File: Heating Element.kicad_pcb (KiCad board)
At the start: 2 copper layers, 56 x 37 mm, 20 parts, among them IC1 UCC23513QDWYRQ1, J1 Conn_01x04_Pin, U1 STP55NF06L, U2 MC7815CDTRKG

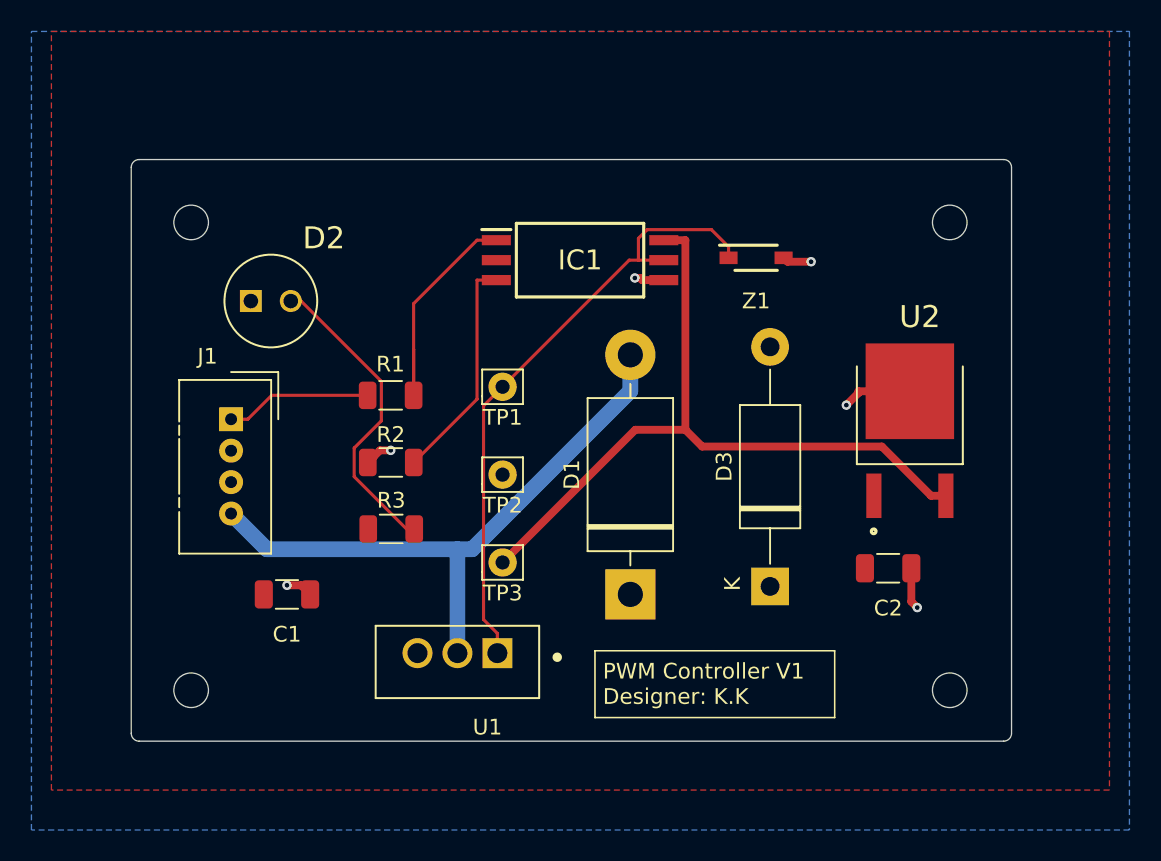
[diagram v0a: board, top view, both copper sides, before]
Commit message: Updated schematic and PCB
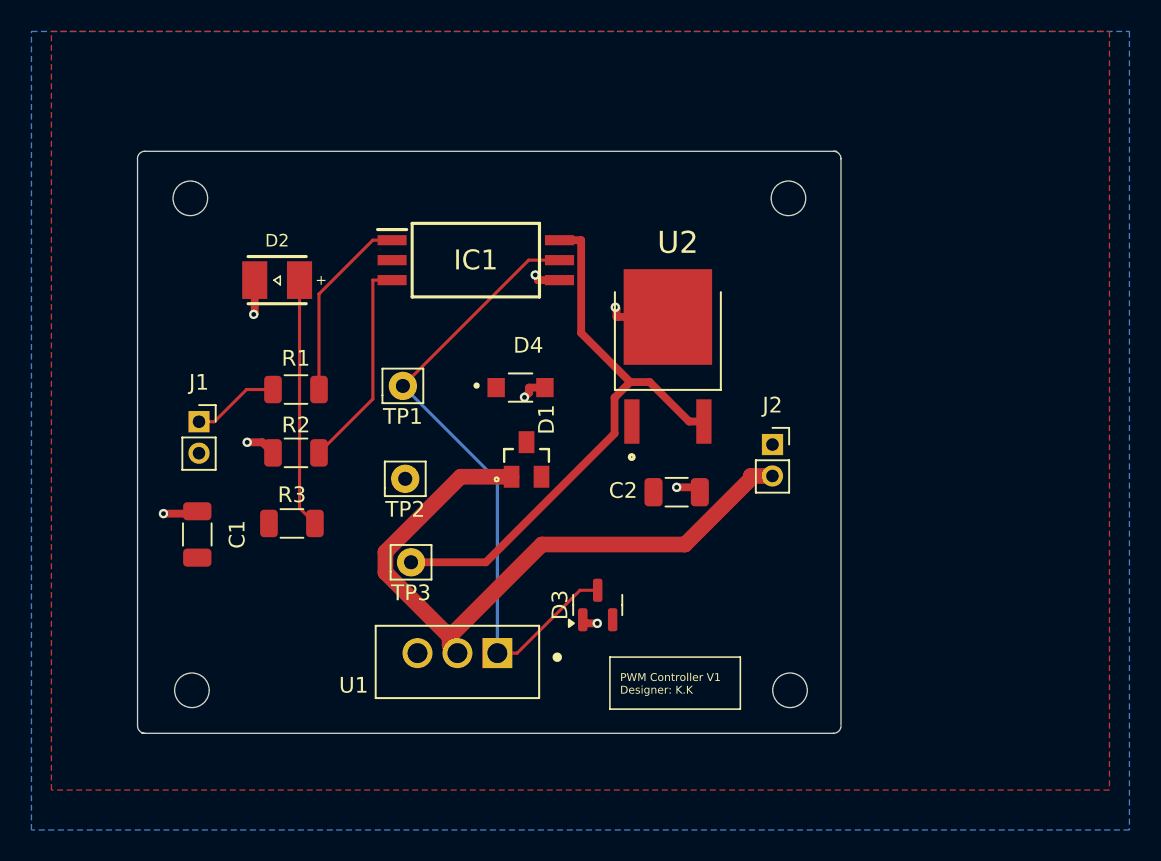
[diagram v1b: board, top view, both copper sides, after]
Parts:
- removed Z1: SZMMSZ5245BT1G, SZMMSZ5245BT1G_Kicad:SOD3716X135N
- added D4: BZD27C24P R3G, BZD27C10P:SODFL3618X143N, F.Cu at (120.0, 92.5)
- added J2: Conn_01x02_Pin, Connector_PinSocket_2.00mm:PinSocket_1x02_P2.00mm_Vertical, F.Cu at (136.0, 96.1)
- D1: value D -> PMEG3005ET-QR; footprint Diode_THT:D_DO-201AD_P15.24mm_Horizontal -> BAS70-7:SOT23
- D2: value L-53GD -> KA-3528SGT; footprint L-53GD:LEDRD254W50D500H1060 -> WL-SMTW_3528:WL-SMTW_3528
- D3: value D_Zener -> BZX84C15; footprint Diode_THT:D_DO-15_P15.24mm_Horizontal -> Package_TO_SOT_SMD:SOT-23
- J1: value Conn_01x04_Pin -> Conn_01x02_Pin; footprint Connector:NS-Tech_Grove_1x04_P2mm_Vertical -> Connector_PinSocket_2.00mm:PinSocket_1x02_P2.00mm_Vertical
- moved U2 16.1 mm to (129.4, 90.5)
- moved C2 14.3 mm to (129.9, 99.2)
- moved D3 11.0 mm to (124.9, 106.3)
- moved D1 10.8 mm to (120.4, 97.1)
- moved H2 10.4 mm to (137.1, 80.5)
- moved H4 10.2 mm to (137.2, 111.8)
- moved C1 6.86 mm to (99.5, 101.8), turned to 90 degrees
- moved IC1 6.63 mm to (117.2, 84.4)
- moved TP1 6.34 mm to (112.5, 92.4)
- moved R3 6.32 mm to (105.5, 101.2)
- moved TP2 6.20 mm to (112.7, 98.3)
- moved R2 6.06 mm to (105.7, 96.7)
- moved R1 6.03 mm to (105.7, 92.6)
- moved TP3 5.82 mm to (113.0, 103.6)
- moved J1 2.05 mm to (99.6, 94.7)
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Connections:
- D1 pad 1: +24V -> /Vdrain
- D1 pad 2: /Vdrain -> unconnected-(D1-Pad2)
- D3 pad 1: +24V -> GND
- D3 pad 2: GND -> unconnected-(D3-NC-Pad2)
- R3 pad 2: Net-(D2-PadA) -> Net-(D2-Pad2)
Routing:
- net Net-(D2-PadA): track 19.9 -> 0.00 mm
- net Net-(D2-Pad2): track 0.00 -> 15.9 mm
- net /+15V: track 46.9 -> 37.4 mm
- net /Vdrain: track 39.4 -> 43.2 mm
- net /PWM input: track 9.32 -> 5.56 mm
- net Net-(IC1-ANODE): track 15.7 -> 12.1 mm
- net GND: track 14.9 -> 16.5 mm, vias 6 -> 8
- net /VG: track 39.9 -> 40.8 mm
- net Net-(IC1-CATHODE): track 14.5 -> 13.6 mm
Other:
- board size 56 x 37 mm -> 44.8 x 37 mm

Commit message: Updated Schematic components (all smd) Updated PCB layout (includes schematic changes and routing) Updtaed Gerber files
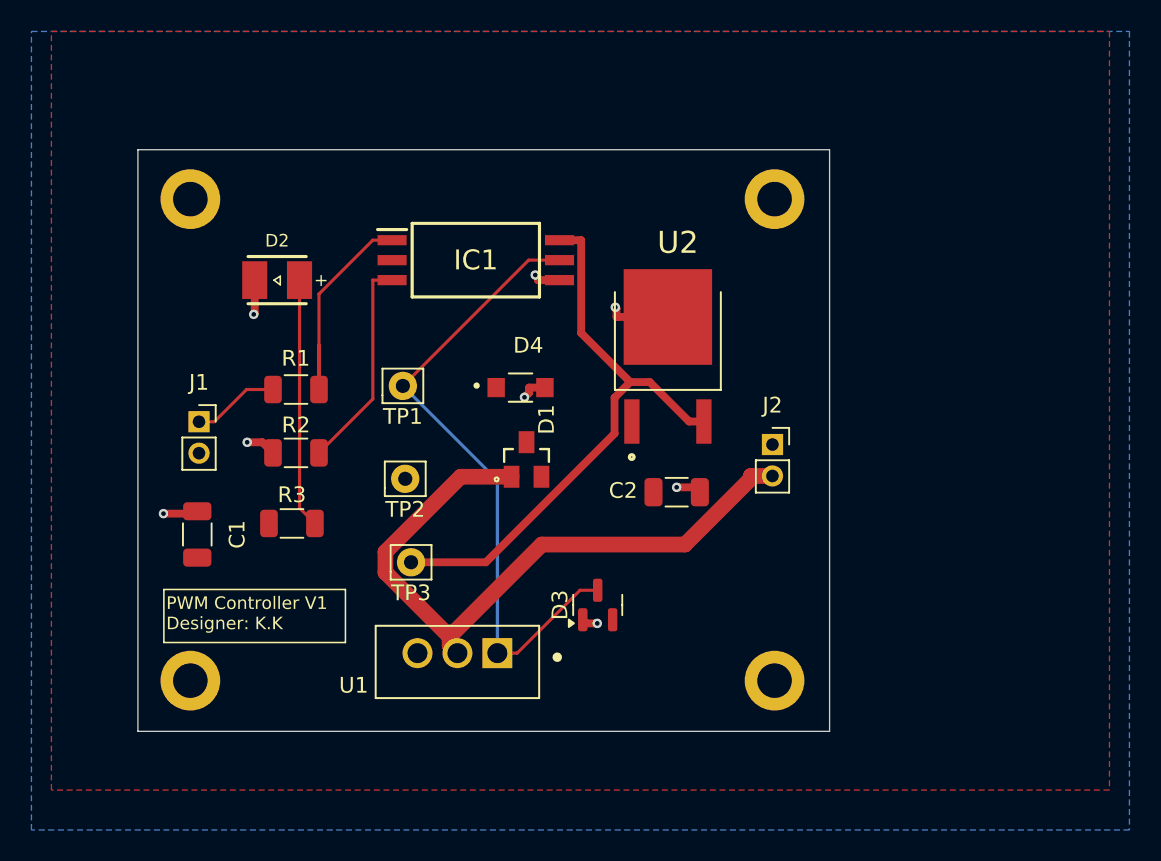
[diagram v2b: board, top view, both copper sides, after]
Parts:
- H1, H2, H3, H4: value MountingHole -> MountingHole_Pad_MP; footprint MountingHole:MountingHole_2.2mm_M2 -> MountingHole:MountingHole_2.2mm_M2_DIN965_Pad
- moved H4 1.16 mm to (136.2, 111.2)
- moved H2 0.88 mm to (136.2, 80.5)
- moved H3 0.62 mm to (99.0, 111.2)
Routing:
- net Net-(IC1-ANODE): track 12.1 -> 15.0 mm
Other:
- board size 44.8 x 37 mm -> 44 x 37 mm

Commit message: updated Heating PCB
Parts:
- removed TP1, TP2, TP3: TestPoint, Connector_Pin:Pin_D0.9mm_L10.0mm_W2.4mm_FlatFork
- added +15V_TP1: TestPoint, Connector_Pin:Pin_D0.9mm_L10.0mm_W2.4mm_FlatFork, F.Cu at (112.9, 91.7)
- added GND_TP1: TestPoint, Connector_Pin:Pin_D0.9mm_L10.0mm_W2.4mm_FlatFork, F.Cu at (112.9, 95.5)
- added R4: 1.1k, Resistor_SMD:R_1206_3216Metric, F.Cu at (112.6, 105.1)
- added R5: 15k, Resistor_SMD:R_1206_3216Metric, F.Cu at (118.7, 96.2)
- added R6: 1.1k, Resistor_SMD:R_1206_3216Metric, F.Cu at (122.9, 96.2)
- added VG_TP1: TestPoint, Connector_Pin:Pin_D0.9mm_L10.0mm_W2.4mm_FlatFork, F.Cu at (112.9, 99.4)
- J1: value Conn_01x02_Pin -> Conn_01x04_Pin; footprint Connector_PinSocket_2.00mm:PinSocket_1x02_P2.00mm_Vertical -> Connector_PinSocket_2.54mm:PinSocket_1x04_P2.54mm_Vertical
- J2: footprint Connector_PinSocket_2.00mm:PinSocket_1x02_P2.00mm_Vertical -> Connector_PinHeader_2.54mm:PinHeader_1x02_P2.54mm_Vertical
- R3: value 1.1k -> 2.4k
- moved C2 6.83 mm to (123.7, 101.8)
- moved D1 6.77 mm to (127.2, 96.6)
- moved J1 5.48 mm to (98.8, 89.2)
- moved U2 3.37 mm to (130.0, 87.2)
- moved R3 2.50 mm to (106.9, 99.1)
- moved R1 2.50 mm to (107.2, 90.6)
- moved R2 2.50 mm to (107.2, 94.6)
- moved D4 2.49 mm to (122.5, 92.0)
- moved D2 2.32 mm to (105.7, 83.7)
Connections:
- D1 pad 3: +24V -> Net-(D1-Pad3)
- D3 pad 3: /VG -> Net-(D3-K)
- D4 pad 1: +24V -> Net-(D4-Pad1)
- R3 pad 2: Net-(D2-Pad2) -> Net-(D1-Pad3)
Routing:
- net Net-(D1-Pad3): track 0.00 -> 21.8 mm
- net /Vdrain: track 43.2 -> 27.4 mm, vias 0 -> 1
- net Net-(D3-K): track 0.00 -> 13.8 mm
- net Net-(D2-Pad2): track 15.9 -> 26.3 mm, vias 0 -> 2
- net /+15V: track 37.4 -> 28.8 mm
- net Net-(IC1-ANODE): track 15.0 -> 9.51 mm
- net Net-(D4-Pad1): track 0.00 -> 3.64 mm
- net /VG: track 40.8 -> 43.5 mm, vias 0 -> 1
- net Net-(IC1-CATHODE): track 13.6 -> 11.0 mm
- net /PWM input: track 5.56 -> 7.48 mm
- net GND: track 16.9 -> 16.2 mm
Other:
- board text added: "PWM Controller V2 Designer: K.K"
- board text removed: "PWM Controller V1 Designer: K.K"
